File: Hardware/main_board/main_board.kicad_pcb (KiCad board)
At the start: 6 copper layers, 95.4 x 36.1 mm, 237 parts, among them J1 BATT, J2 LCD, J3 BACK_LIGHT, J4 SD, J5 NFC, J6 EXT1, J7 EXT0, J8 USB_C, Q1 DMN313DLT, SW1 OK, SW2 BACK, SW3 RIGHT, SW4 LEFT, SW5 UP, SW6 DOWN, T1 B0310J50100AHF, U1 STM32WB55RGVx, U10 BGS13S4N9E6327XTSA1, U11 NC7SZ32M5X, U12 LP5562TMX, U2 BQ27220YZFR, U3 BQ25896RTWR, U4 RS3221-3.3YF3, U5 LM66100DCK, U6 LM3281YFQR, U7 LM3281YFQR, U8 CC1101RGP, U9 BGS13S4N9E6327XTSA1, Y1 32MHz, Y2 32.768K, Y3 26MHz

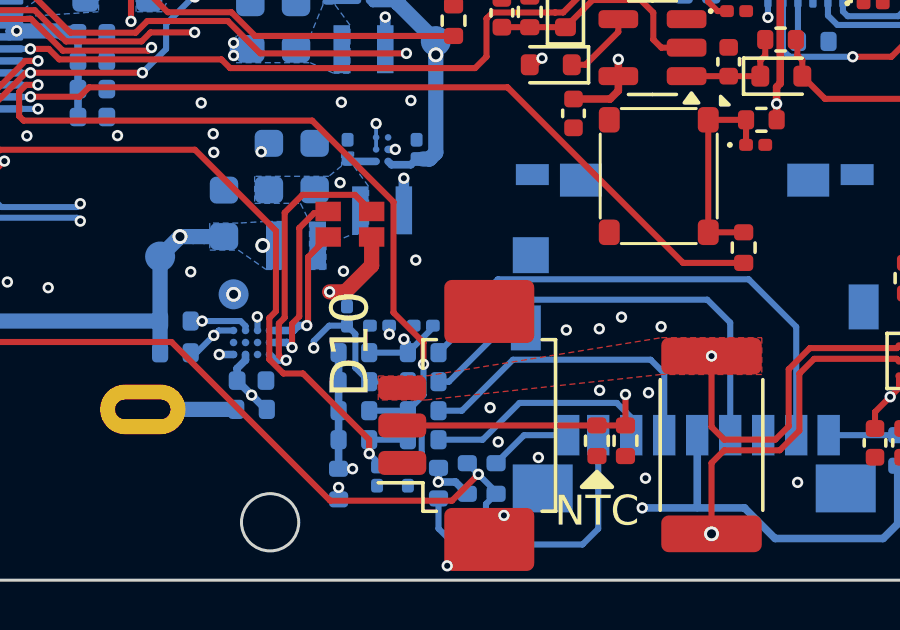
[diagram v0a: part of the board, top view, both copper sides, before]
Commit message: layout: change LED footprint
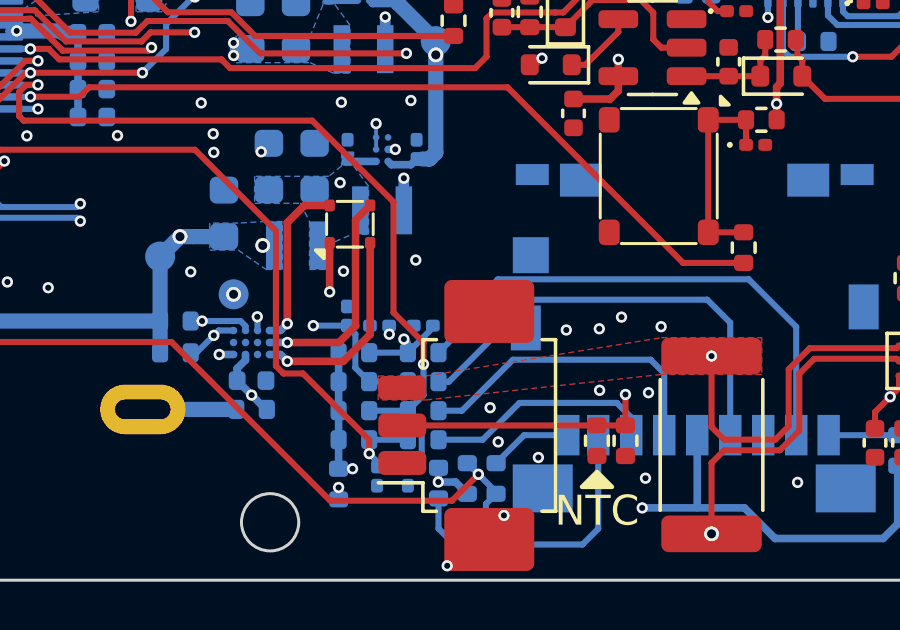
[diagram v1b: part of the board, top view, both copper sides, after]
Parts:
- D10: value LTST-C19HE1WT -> LED_ABGR; footprint Library:LTST-C19HE1WT -> Library:LED_PLCC-4_1.5x1.5mm_CW
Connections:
- D10 pad 1: Net-(D10-RED) -> VSYS
- D10 pad 2: Net-(D10-GREEN) -> Net-(D10-BK)
- D10 pad 3: Net-(D10-BLUE) -> Net-(D10-GK)
- D10 pad 4: VSYS -> Net-(D10-RK)
- U12 pad A4: Net-(D10-BLUE) -> Net-(D10-BK)
- U12 pad B4: Net-(D10-GREEN) -> Net-(D10-GK)
- U12 pad C4: Net-(D10-RED) -> Net-(D10-RK)
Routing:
- net Net-(D10-BLUE): track 9.23 -> 0.00 mm, vias 1 -> 0
- net Net-(D10-GK): track 0.00 -> 7.31 mm, vias 0 -> 1
- net Net-(D10-BK): track 0.00 -> 6.87 mm, vias 0 -> 1
- net Net-(D10-GREEN): track 6.18 -> 0.00 mm, vias 1 -> 0
- net Net-(D10-RK): track 0.00 -> 5.71 mm, vias 0 -> 1
- net Net-(D10-RED): track 4.56 -> 0.00 mm, vias 1 -> 0
- net VSYS: track 69.9 -> 68.9 mm
- net Net-(J4-DAT3/CD): track 7.13 -> 7.72 mm

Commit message: misc: fix some fields
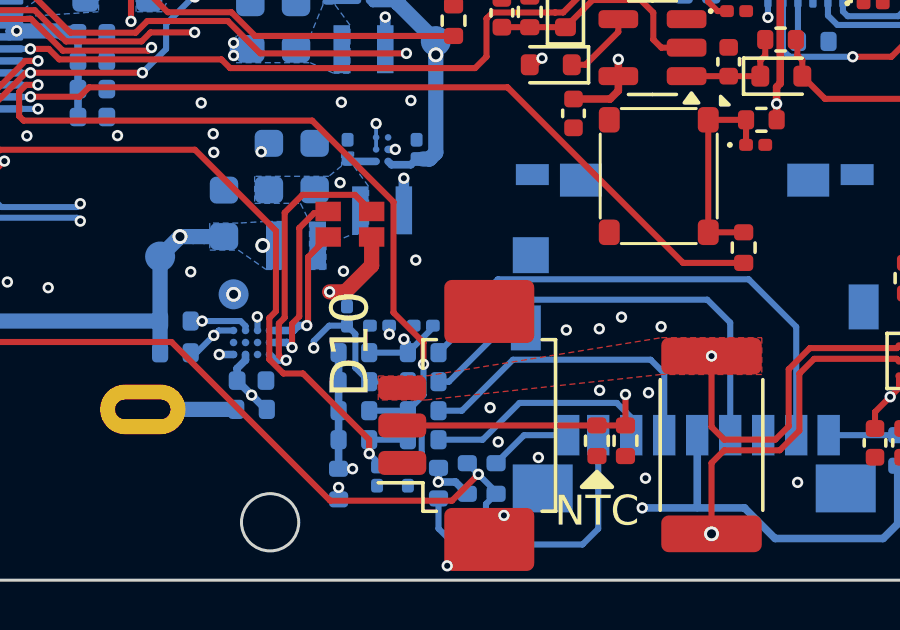
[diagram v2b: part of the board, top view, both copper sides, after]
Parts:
- D10: value LED_ABGR -> LTST-C19HE1WT; footprint Library:LED_PLCC-4_1.5x1.5mm_CW -> Library:LTST-C19HE1WT
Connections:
- D10 pad 1: VSYS -> Net-(D10-RED)
- D10 pad 2: Net-(D10-BK) -> Net-(D10-GREEN)
- D10 pad 3: Net-(D10-GK) -> Net-(D10-BLUE)
- D10 pad 4: Net-(D10-RK) -> VSYS
- U12 pad A4: Net-(D10-BK) -> Net-(D10-BLUE)
- U12 pad B4: Net-(D10-GK) -> Net-(D10-GREEN)
- U12 pad C4: Net-(D10-RK) -> Net-(D10-RED)
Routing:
- net Net-(D10-BLUE): track 0.00 -> 9.23 mm, vias 0 -> 1
- net Net-(D10-GK): track 7.31 -> 0.00 mm, vias 1 -> 0
- net Net-(D10-BK): track 6.87 -> 0.00 mm, vias 1 -> 0
- net Net-(D10-GREEN): track 0.00 -> 6.18 mm, vias 0 -> 1
- net Net-(D10-RK): track 5.71 -> 0.00 mm, vias 1 -> 0
- net Net-(D10-RED): track 0.00 -> 4.56 mm, vias 0 -> 1
- net VSYS: track 68.9 -> 69.9 mm
- net Net-(J4-DAT3/CD): track 7.72 -> 7.13 mm
